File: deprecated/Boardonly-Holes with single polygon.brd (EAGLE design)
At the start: 160 x 201.6 mm, 0 parts

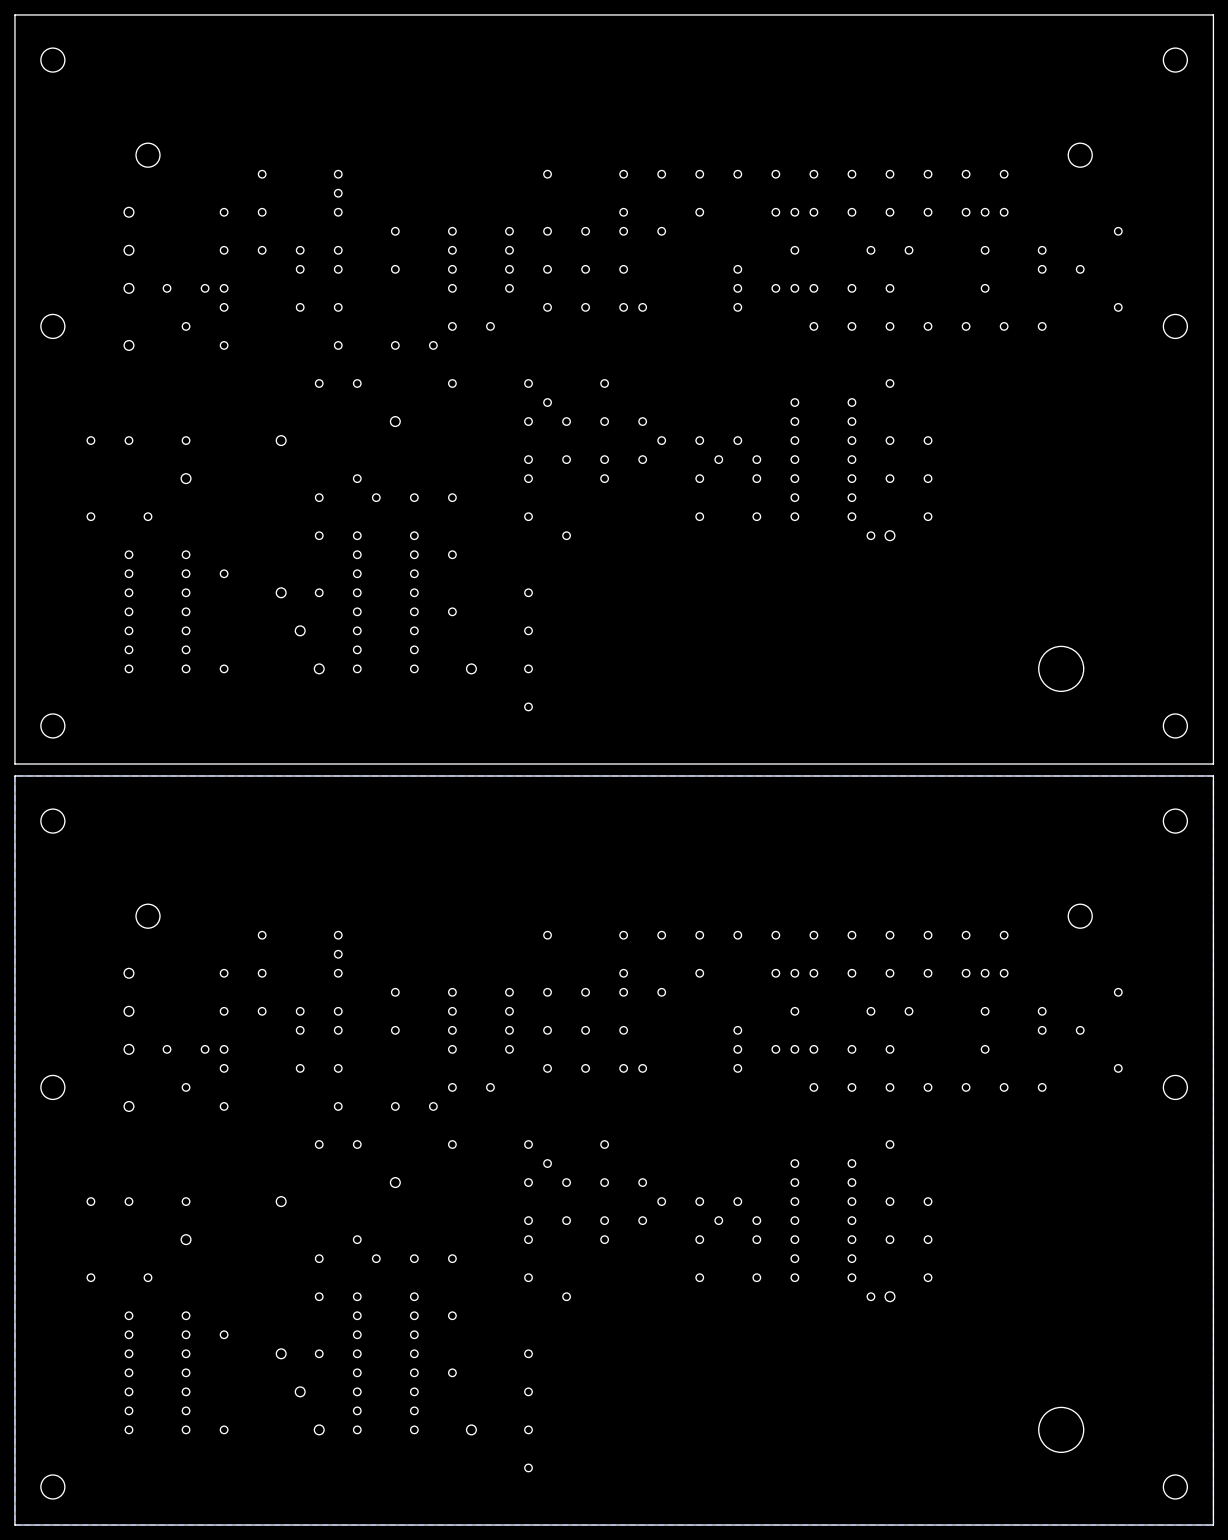
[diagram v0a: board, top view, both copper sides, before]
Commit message: updated LBR and BRD: Solder pin holes are now 1.4mm drills instead of 1.3
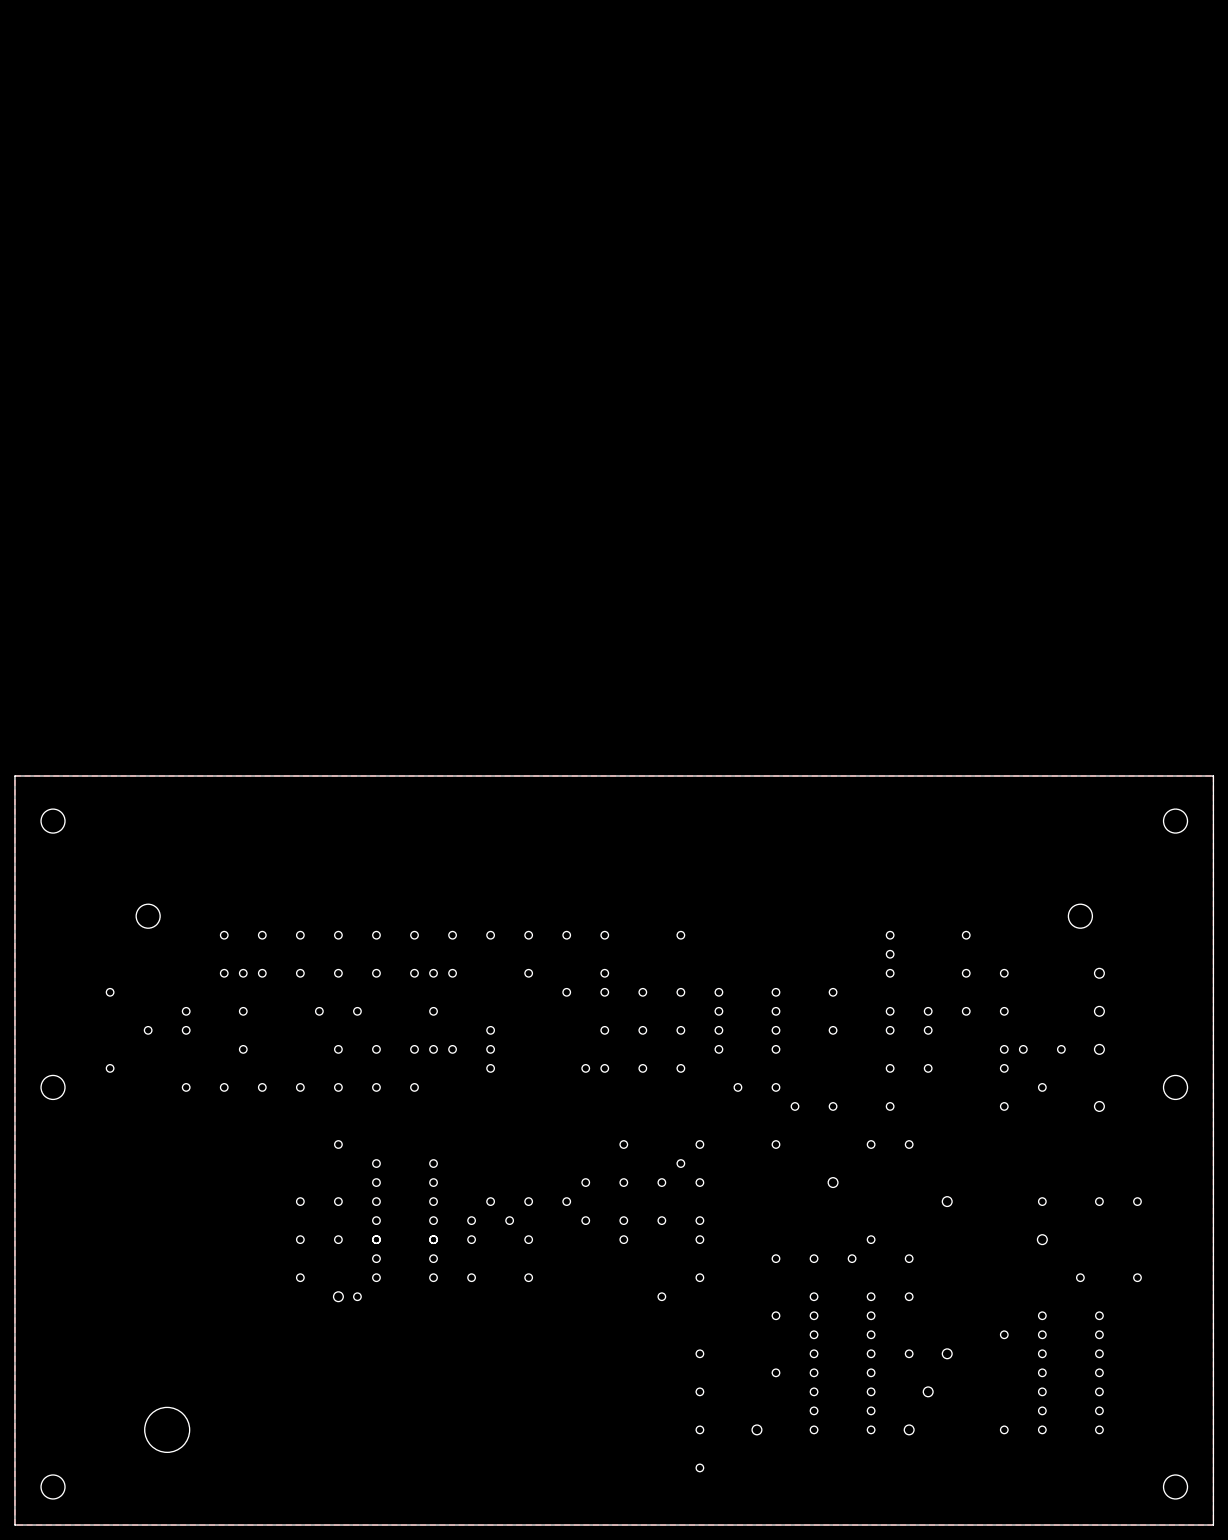
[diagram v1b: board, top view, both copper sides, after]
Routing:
- added copper zone on layer 1, net S$1
- removed copper zone on layer 16, net S$1
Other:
- board size 160 x 201.6 mm -> 160 x 100 mm
